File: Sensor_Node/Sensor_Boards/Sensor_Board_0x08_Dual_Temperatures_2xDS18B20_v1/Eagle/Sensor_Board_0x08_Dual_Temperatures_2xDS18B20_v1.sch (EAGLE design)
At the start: 16 parts, among them J2 1x3 RA Female .1", J3 1x3 RA Female .1", J4 ARDUINO_ISP, U2 ATMEGA328P_TQFP, Y1 8MHZ

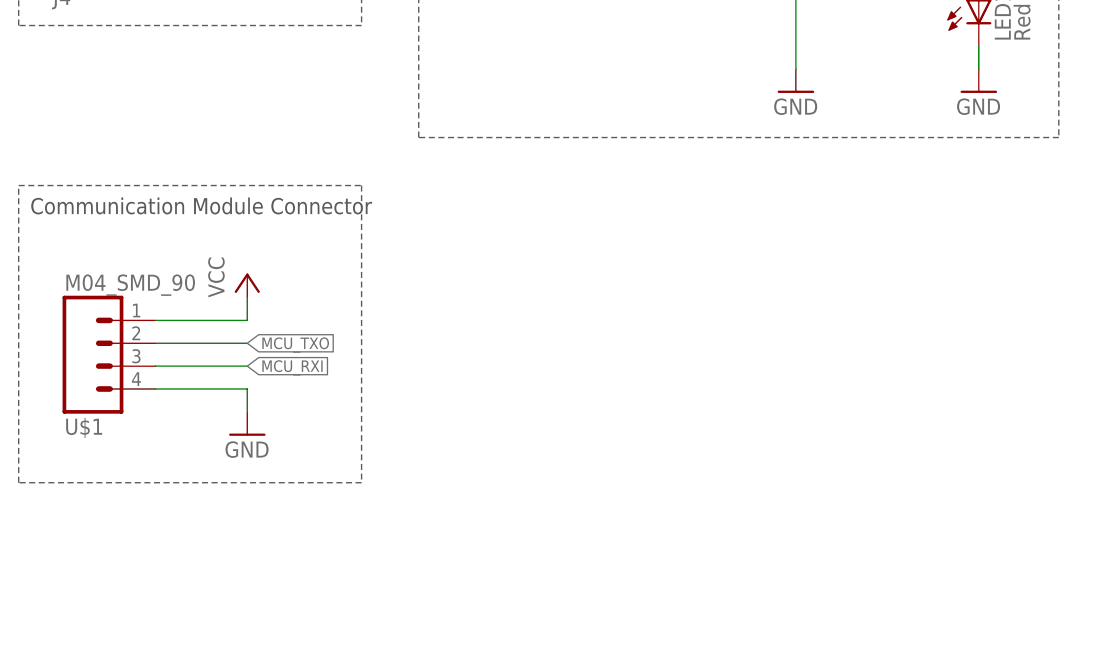
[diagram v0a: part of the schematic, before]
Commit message: Changes on SensModule 2xDS18B20
- added pogopin programming connector
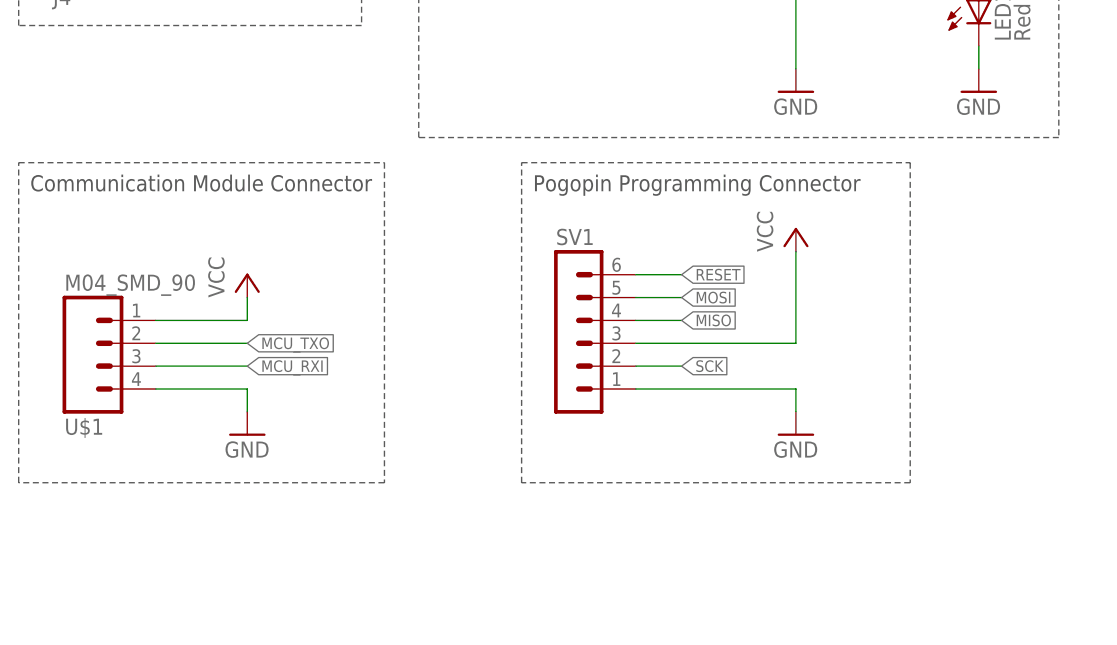
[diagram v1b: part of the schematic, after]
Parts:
- added SV1: (no value), con-lstb:MA06-1
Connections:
- net GND: now also SV1.1
- net MISO: now also SV1.4
- net MOSI: now also SV1.5
- net RESET: now also SV1.6
- net SCK: now also SV1.2
- net VCC: now also SV1.3
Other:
- note added: "Pogopin Programming Connector"
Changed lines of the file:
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@@
 <layers>
 <layer number="1" name="Top" color="4" fill="1" visible="no" active="no"/>
+<layer number="2" name="Route2" color="1" fill="3" visible="no" active="no"/>
+<layer number="3" name="Route3" color="4" fill="3" visible="no" active="no"/>
+<layer number="4" name="Route4" color="1" fill="4" visible="no" active="no"/>
+<layer number="5" name="Route5" color="4" fill="4" visible="no" active="no"/>
+<layer number="6" name="Route6" color="1" fill="8" visible="no" active="no"/>
+<layer number="7" name="Route7" color="4" fill="8" visible="no" active="no"/>
+<layer number="8" name="Route8" color="1" fill="2" visible="no" active="no"/>
+<layer number="9" name="Route9" color="4" fill="2" visible="no" active="no"/>
+<layer number="10" name="Route10" color="1" fill="7" visible="no" active="no"/>
+<layer number="11" name="Route11" color="4" fill="7" visible="no" active="no"/>
+<layer number="12" name="Route12" color="1" fill="5" visible="no" active="no"/>
+<layer number="13" name="Route13" color="4" fill="5" visible="no" active="no"/>
+<layer number="14" name="Route14" color="1" fill="6" visible="no" active="no"/>
+<layer number="15" name="Route15" color="4" fill="6" visible="no" active="no"/>
 <layer number="16" name="Bottom" color="1" fill="1" visible="no" active="no"/>
 <layer number="17" name="Pads" color="2" fill="1" visible="no" active="no"/>
@@
 <part name="U$16" library="myownthings" deviceset="N/C" device=""/>
 <part name="U$17" library="myownthings" deviceset="N/C" device=""/>
+<part name="SV1" library="con-lstb" deviceset="MA06-1" device=""/>
+<part name="P+8" library="supply1" deviceset="VCC" device=""/>
+<part name="GND3" library="SparkFun-Aesthetics" deviceset="GND" device=""/>
 </parts>
 <sheets>
@@
 <wire x1="125.73" y1="200.66" x2="7.62" y2="200.66" width="0.1524" layer="97" style="shortdash"/>
 <text x="8.89" y="197.485" size="1.778" layer="97">ATmega328</text>
-<wire x1="7.62" y1="30.226" x2="7.62" y2="63.246" width="0.1524" layer="97" style="shortdash"/>
-<wire x1="7.62" y1="63.246" x2="45.72" y2="63.246" width="0.1524" layer="97" style="shortdash"/>
-<wire x1="45.72" y1="63.246" x2="45.72" y2="30.226" width="0.1524" layer="97" style="shortdash"/>
-<wire x1="45.72" y1="30.226" x2="7.62" y2="30.226" width="0.1524" layer="97" style="shortdash"/>
-<text x="8.89" y="60.071" size="1.778" layer="97">Communication Module Connector</text>
+<wire x1="7.62" y1="30.226" x2="7.62" y2="65.786" width="0.1524" layer="97" style="shortdash"/>
+<wire x1="7.62" y1="65.786" x2="48.26" y2="65.786" width="0.1524" layer="97" style="shortdash"/>
+<wire x1="48.26" y1="65.786" x2="48.26" y2="30.226" width="0.1524" layer="97" style="shortdash"/>
+<wire x1="48.26" y1="30.226" x2="7.62" y2="30.226" width="0.1524" layer="97" style="shortdash"/>
+<text x="8.89" y="62.611" size="1.778" layer="97">Communication Module Connector</text>
 <wire x1="200.66" y1="152.4" x2="134.62" y2="152.4" width="0.1524" layer="97" style="shortdash"/>
 <wire x1="134.62" y1="88.9" x2="134.62" y2="152.4" width="0.1524" layer="97" style="shortdash"/>
@@
 <text x="224.505775" y="11.52471875" size="2.54" layer="94" font="vector">Sensor Board - 2xDS18B20</text>
 <text x="278.465165625" y="1.12011875" size="2.54" layer="94" font="vector">1.0</text>
+<wire x1="63.5" y1="30.226" x2="63.5" y2="65.786" width="0.1524" layer="97" style="shortdash"/>
+<wire x1="63.5" y1="65.786" x2="106.68" y2="65.786" width="0.1524" layer="97" style="shortdash"/>
+<wire x1="106.68" y1="65.786" x2="106.68" y2="30.226" width="0.1524" layer="97" style="shortdash"/>
+<wire x1="106.68" y1="30.226" x2="63.5" y2="30.226" width="0.1524" layer="97" style="shortdash"/>
+<text x="64.77" y="62.611" size="1.778" layer="97">Pogopin Programming Connector</text>
 </plain>
 <instances>
@@
 <instance part="U$16" gate="G$1" x="106.68" y="91.44"/>
 <instance part="U$17" gate="G$1" x="106.68" y="88.9"/>
+<instance part="SV1" gate="1" x="68.58" y="48.26"/>
+<instance part="P+8" gate="VCC" x="93.98" y="58.42"/>
+<instance part="GND3" gate="1" x="93.98" y="35.56"/>
 </instances>
 <busses>
@@
 <junction x="33.02" y="132.08"/>
 <junction x="33.02" y="129.54"/>
+</segment>
+<segment>
+<pinref part="SV1" gate="1" pin="1"/>
+<pinref part="GND3" gate="1" pin="GND"/>
+<wire x1="76.2" y1="40.64" x2="93.98" y2="40.64" width="0.1524" layer="91"/>
+<wire x1="93.98" y1="40.64" x2="93.98" y2="38.1" width="0.1524" layer="91"/>
 </segment>
 </net>
@@
 <wire x1="93.98" y1="93.98" x2="96.52" y2="93.98" width="0.1524" layer="91"/>
 </segment>
+<segment>
+<pinref part="P+8" gate="VCC" pin="VCC"/>
+<wire x1="93.98" y1="55.88" x2="93.98" y2="45.72" width="0.1524" layer="91"/>
+<pinref part="SV1" gate="1" pin="3"/>
+<wire x1="93.98" y1="45.72" x2="76.2" y2="45.72" width="0.1524" layer="91"/>
+</segment>
 </net>
 <net name="RESET" class="0">
@@
 <pinref part="J4" gate="G$1" pin="RST"/>
 </segment>
+<segment>
+<pinref part="SV1" gate="1" pin="6"/>
+<wire x1="76.2" y1="53.34" x2="81.28" y2="53.34" width="0.1524" layer="91"/>
+<label x="81.28" y="53.34" size="1.27" layer="95" xref="yes"/>
+</segment>
 </net>
 <net name="SCK" class="0">
@@
 <pinref part="U2" gate="U$1" pin="PB5(SCK)"/>
 </segment>
+<segment>
+<pinref part="SV1" gate="1" pin="2"/>
+<wire x1="76.2" y1="43.18" x2="81.28" y2="43.18" width="0.1524" layer="91"/>
+<label x="81.28" y="43.18" size="1.27" layer="95" xref="yes"/>
+</segment>
 </net>
 <net name="MISO" class="0">
@@
 <pinref part="U2" gate="U$1" pin="PB4(MISO)"/>
 </segment>
+<segment>
+<pinref part="SV1" gate="1" pin="4"/>
+<wire x1="76.2" y1="48.26" x2="81.28" y2="48.26" width="0.1524" layer="91"/>
+<label x="81.28" y="48.26" size="1.27" layer="95" xref="yes"/>
+</segment>
 </net>
 <net name="MOSI" class="0">
@@
 <pinref part="U2" gate="U$1" pin="PB3(MOSI/OC2)"/>
 </segment>
+<segment>
+<pinref part="SV1" gate="1" pin="5"/>
+<wire x1="76.2" y1="50.8" x2="81.28" y2="50.8" width="0.1524" layer="91"/>
+<label x="81.28" y="50.8" size="1.27" layer="95" xref="yes"/>
+</segment>
 </net>

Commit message: Changes on all boards
- added capacitor on reset-path
- changed order of pogopin programmer pins

Pulse-Board:
- Deleted input-jumper. Currently one interrupt-pin missing, so print is
not yet routed.
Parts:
- added C1: 100n, eagle-ltspice:C
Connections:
- new net N$4: C1.2, R5.1, S1.RIGHT, U2.PC6(/RESET)
- net MISO: now also SV1.6; no longer SV1.4
- net MOSI: now also SV1.2; no longer SV1.5
- net RESET: now also C1.1, SV1.4; no longer R5.1, S1.RIGHT, SV1.6, U2.PC6(/RESET)
- net SCK: now also SV1.5; no longer SV1.2
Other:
- moved on the sheet: C10, C9, R5, S1, U2, Y1

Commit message: Updated schematic description
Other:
- note added: "Sensor Board - 2xDS18B20 (0x08)"
- note removed: "Sensor Board - 2xDS18B20"
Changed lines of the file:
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@@
 <wire x1="200.66" y1="88.9" x2="134.62" y2="88.9" width="0.1524" layer="97" style="shortdash"/>
 <text x="137.16" y="147.32" size="1.778" layer="97">DS18B20</text>
-<text x="224.505775" y="11.52471875" size="2.54" layer="94" font="vector">Sensor Board - 2xDS18B20</text>
+<text x="224.505775" y="11.52471875" size="2.54" layer="94" font="vector">Sensor Board - 2xDS18B20 (0x08)</text>
 <text x="278.465165625" y="1.12011875" size="2.54" layer="94" font="vector">1.0</text>
 <wire x1="63.5" y1="30.226" x2="63.5" y2="65.786" width="0.1524" layer="97" style="shortdash"/>

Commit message: Finished some boards.
- Minor changes on all boards except
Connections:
- new net FTDI_RXI: SV1.4, U2.PD0(RXD)
- new net FTDI_TXO: SV1.5, U2.PD1(TXD)
- net GND: now also SV1.2
- net MCU_RXI: now also U2.PD7(AIN1); no longer U2.PD0(RXD)
- net MCU_TXO: now also U2.PD6(AIN0); no longer U2.PD1(TXD)
- net MISO: no longer SV1.6
- net MOSI: no longer SV1.2
- net RESET: now also SV1.6; no longer SV1.4
- net SCK: no longer SV1.5
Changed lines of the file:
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@@
 <setting verticaltext="up"/>
 </settings>
-<grid distance="0.1" unitdist="inch" unit="inch" style="lines" multiple="1" display="no" altdistance="0.01" altunitdist="inch" altunit="inch"/>
+<grid distance="0.05" unitdist="inch" unit="inch" style="lines" multiple="1" display="yes" altdistance="0.01" altunitdist="inch" altunit="inch"/>
 <layers>
 <layer number="1" name="Top" color="4" fill="1" visible="no" active="no"/>
@@
 <part name="U$8" library="myownthings" deviceset="N/C" device=""/>
 <part name="U$9" library="myownthings" deviceset="N/C" device=""/>
-<part name="U$10" library="myownthings" deviceset="N/C" device=""/>
-<part name="U$11" library="myownthings" deviceset="N/C" device=""/>
 <part name="U$12" library="myownthings" deviceset="N/C" device=""/>
 <part name="U$13" library="myownthings" deviceset="N/C" device=""/>
@@
 <wire x1="45.72" y1="81.026" x2="7.62" y2="81.026" width="0.1524" layer="97" style="shortdash"/>
 <text x="8.89" y="110.871" size="1.778" layer="97">Programming Connector</text>
-<wire x1="6.35" y1="204.47" x2="7.62" y2="118.11" width="0.1524" layer="97" style="shortdash"/>
-<wire x1="7.62" y1="118.11" x2="125.73" y2="118.11" width="0.1524" layer="97" style="shortdash"/>
-<wire x1="125.73" y1="118.11" x2="124.46" y2="204.47" width="0.1524" layer="97" style="shortdash"/>
-<wire x1="124.46" y1="204.47" x2="6.35" y2="204.47" width="0.1524" layer="97" style="shortdash"/>
+<wire x1="7.62" y1="204.47" x2="7.62" y2="118.11" width="0.1524" layer="97" style="shortdash"/>
+<wire x1="7.62" y1="118.11" x2="124.46" y2="118.11" width="0.1524" layer="97" style="shortdash"/>
+<wire x1="124.46" y1="118.11" x2="124.46" y2="204.47" width="0.1524" layer="97" style="shortdash"/>
+<wire x1="124.46" y1="204.47" x2="7.62" y2="204.47" width="0.1524" layer="97" style="shortdash"/>
 <text x="8.89" y="201.295" size="1.778" layer="97">ATmega328</text>
 <wire x1="7.62" y1="30.226" x2="7.62" y2="65.786" width="0.1524" layer="97" style="shortdash"/>
@@
 <instance part="U$8" gate="G$1" x="102.87" y="156.21"/>
 <instance part="U$9" gate="G$1" x="102.87" y="153.67"/>
-<instance part="U$10" gate="G$1" x="102.87" y="151.13"/>
-<instance part="U$11" gate="G$1" x="102.87" y="148.59"/>
 <instance part="U$12" gate="G$1" x="102.87" y="146.05"/>
 <instance part="U$13" gate="G$1" x="102.87" y="143.51"/>
@@
 <wire x1="76.2" y1="40.64" x2="93.98" y2="40.64" width="0.1524" layer="91"/>
 <wire x1="93.98" y1="40.64" x2="93.98" y2="38.1" width="0.1524" layer="91"/>
+<pinref part="SV1" gate="1" pin="2"/>
+<wire x1="76.2" y1="43.18" x2="93.98" y2="43.18" width="0.1524" layer="91"/>
+<wire x1="93.98" y1="43.18" x2="93.98" y2="40.64" width="0.1524" layer="91"/>
+<junction x="93.98" y="40.64"/>
 </segment>
 </net>
@@
 </segment>
 <segment>
-<pinref part="SV1" gate="1" pin="4"/>
-<wire x1="76.2" y1="48.26" x2="81.28" y2="48.26" width="0.1524" layer="91"/>
-<label x="81.28" y="48.26" size="1.27" layer="95" xref="yes"/>
+<pinref part="SV1" gate="1" pin="6"/>
+<wire x1="76.2" y1="53.34" x2="81.28" y2="53.34" width="0.1524" layer="91"/>
+<label x="81.28" y="53.34" size="1.27" layer="95" xref="yes"/>
 </segment>
 </net>
@@
 <pinref part="U2" gate="U$1" pin="PB5(SCK)"/>
 </segment>
-<segment>
-<pinref part="SV1" gate="1" pin="5"/>
-<wire x1="76.2" y1="50.8" x2="81.28" y2="50.8" width="0.1524" layer="91"/>
-<label x="81.28" y="50.8" size="1.27" layer="95" xref="yes"/>
-</segment>
 </net>
 <net name="MISO" class="0">
@@
 <pinref part="U2" gate="U$1" pin="PB4(MISO)"/>
 </segment>
-<segment>
-<pinref part="SV1" gate="1" pin="6"/>
-<wire x1="76.2" y1="53.34" x2="81.28" y2="53.34" width="0.1524" layer="91"/>
-<label x="81.28" y="53.34" size="1.27" layer="95" xref="yes"/>
-</segment>
 </net>
 <net name="MOSI" class="0">
@@
 <pinref part="U2" gate="U$1" pin="PB3(MOSI/OC2)"/>
 </segment>
-<segment>
-<pinref part="SV1" gate="1" pin="2"/>
-<wire x1="76.2" y1="43.18" x2="81.28" y2="43.18" width="0.1524" layer="91"/>
-<label x="81.28" y="43.18" size="1.27" layer="95" xref="yes"/>
-</segment>
 </net>
 <net name="MCU_TXO" class="0">
-<segment>
-<wire x1="102.87" y1="163.83" x2="105.41" y2="163.83" width="0.1524" layer="91"/>
-<label x="105.41" y="163.83" size="1.27" layer="95" xref="yes"/>
-<pinref part="U2" gate="U$1" pin="PD1(TXD)"/>
-</segment>
 <segment>
 <label x="33.02" y="45.72" size="1.27" layer="95" xref="yes"/>
@@
 <wire x1="33.02" y1="45.72" x2="22.86" y2="45.72" width="0.1524" layer="91"/>
 </segment>
+<segment>
+<pinref part="U2" gate="U$1" pin="PD6(AIN0)"/>
+<wire x1="102.87" y1="151.13" x2="105.41" y2="151.13" width="0.1524" layer="91"/>
+<label x="105.41" y="151.13" size="1.27" layer="95" xref="yes"/>
+</segment>
 </net>
 <net name="L1" class="0">
@@
 <net name="MCU_RXI" class="0">
 <segment>
-<wire x1="102.87" y1="166.37" x2="105.41" y2="166.37" width="0.1524" layer="91"/>
-<label x="105.41" y="166.37" size="1.27" layer="95" xref="yes"/>
-<pinref part="U2" gate="U$1" pin="PD0(RXD)"/>
-</segment>
-<segment>
 <label x="33.02" y="43.18" size="1.27" layer="95" xref="yes"/>
 <pinref part="U$1" gate="G$1" pin="3"/>
 <wire x1="33.02" y1="43.18" x2="22.86" y2="43.18" width="0.1524" layer="91"/>
+</segment>
+<segment>
+<pinref part="U2" gate="U$1" pin="PD7(AIN1)"/>
+<wire x1="102.87" y1="148.59" x2="105.41" y2="148.59" width="0.1524" layer="91"/>
+<label x="105.41" y="148.59" size="1.27" layer="95" xref="yes"/>
 </segment>
 </net>
@@
 </segment>
 </net>
+<net name="FTDI_TXO" class="0">
+<segment>
+<pinref part="SV1" gate="1" pin="5"/>
+<wire x1="76.2" y1="50.8" x2="81.28" y2="50.8" width="0.1524" layer="91"/>
+<label x="81.28" y="50.8" size="1.27" layer="95" xref="yes"/>
+</segment>
+<segment>
+<wire x1="102.87" y1="163.83" x2="105.41" y2="163.83" width="0.1524" layer="91"/>
+<label x="105.41" y="163.83" size="1.27" layer="95" xref="yes"/>
+<pinref part="U2" gate="U$1" pin="PD1(TXD)"/>
+</segment>
+</net>
+<net name="FTDI_RXI" class="0">
+<segment>
+<pinref part="SV1" gate="1" pin="4"/>
+<wire x1="76.2" y1="48.26" x2="81.28" y2="48.26" width="0.1524" layer="91"/>
+<label x="81.28" y="48.26" size="1.27" layer="95" xref="yes"/>
+</segment>
+<segment>
+<wire x1="102.87" y1="166.37" x2="105.41" y2="166.37" width="0.1524" layer="91"/>
+<label x="105.41" y="166.37" size="1.27" layer="95" xref="yes"/>
+<pinref part="U2" gate="U$1" pin="PD0(RXD)"/>
+</segment>
+</net>

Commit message: DS18B20 - Board
- adjusted reset path
- minor changes in layout
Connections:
- removed net N$4: C1.2, R5.1, S1.RIGHT, U2.PC6(/RESET)
- new net FTDI_RESET: C1.1, SV1.6
- net RESET: now also C1.2, R5.1, S1.RIGHT, U2.PC6(/RESET); no longer C1.1, SV1.6
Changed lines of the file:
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@@
 <?xml version="1.0" encoding="utf-8"?>
 <!DOCTYPE eagle SYSTEM "eagle.dtd">
-<eagle version="8.1.1">
+<eagle version="8.2.2">
 <drawing>
 <settings>
@@
 <setting verticaltext="up"/>
 </settings>
-<grid distance="0.05" unitdist="inch" unit="inch" style="lines" multiple="1" display="yes" altdistance="0.01" altunitdist="inch" altunit="inch"/>
+<grid distance="0.1" unitdist="inch" unit="inch" style="lines" multiple="1" display="no" altdistance="0.01" altunitdist="inch" altunit="inch"/>
 <layers>
 <layer number="1" name="Top" color="4" fill="1" visible="no" active="no"/>
@@
 </segment>
 <segment>
-<pinref part="C1" gate="G$1" pin="1"/>
-<wire x1="27.94" y1="186.69" x2="22.86" y2="186.69" width="0.1524" layer="91"/>
-<label x="22.86" y="186.69" size="1.778" layer="95" rot="R180" xref="yes"/>
-</segment>
-<segment>
-<pinref part="SV1" gate="1" pin="6"/>
-<wire x1="76.2" y1="53.34" x2="81.28" y2="53.34" width="0.1524" layer="91"/>
-<label x="81.28" y="53.34" size="1.27" layer="95" xref="yes"/>
+<pinref part="R5" gate="G$1" pin="1"/>
+<pinref part="S1" gate="G$1" pin="RIGHT"/>
+<wire x1="41.91" y1="189.23" x2="41.91" y2="186.69" width="0.1524" layer="91"/>
+<pinref part="U2" gate="U$1" pin="PC6(/RESET)"/>
+<wire x1="41.91" y1="186.69" x2="41.91" y2="184.15" width="0.1524" layer="91"/>
+<wire x1="54.61" y1="186.69" x2="48.895" y2="186.69" width="0.1524" layer="91"/>
+<junction x="41.91" y="186.69"/>
+<pinref part="C1" gate="G$1" pin="2"/>
+<wire x1="48.895" y1="186.69" x2="41.91" y2="186.69" width="0.1524" layer="91"/>
+<wire x1="41.91" y1="186.69" x2="35.56" y2="186.69" width="0.1524" layer="91"/>
+<wire x1="48.895" y1="186.69" x2="48.895" y2="194.691" width="0.1524" layer="91"/>
+<junction x="48.895" y="186.69"/>
+<wire x1="48.895" y1="194.691" x2="57.658" y2="194.691" width="0.1524" layer="91"/>
+<wire x1="57.658" y1="194.691" x2="57.658" y2="194.564" width="0.1524" layer="91"/>
+<label x="57.658" y="194.564" size="1.27" layer="95" xref="yes"/>
 </segment>
 </net>
@@
 </segment>
 </net>
-<net name="N$4" class="0">
-<segment>
-<pinref part="R5" gate="G$1" pin="1"/>
-<pinref part="S1" gate="G$1" pin="RIGHT"/>
-<wire x1="41.91" y1="189.23" x2="41.91" y2="186.69" width="0.1524" layer="91"/>
-<pinref part="U2" gate="U$1" pin="PC6(/RESET)"/>
-<wire x1="41.91" y1="186.69" x2="41.91" y2="184.15" width="0.1524" layer="91"/>
-<wire x1="54.61" y1="186.69" x2="41.91" y2="186.69" width="0.1524" layer="91"/>
-<junction x="41.91" y="186.69"/>
-<pinref part="C1" gate="G$1" pin="2"/>
-<wire x1="41.91" y1="186.69" x2="35.56" y2="186.69" width="0.1524" layer="91"/>
-</segment>
-</net>
 <net name="FTDI_TXO" class="0">
 <segment>
@@
 </segment>
 </net>
+<net name="FTDI_RESET" class="0">
+<segment>
+<pinref part="SV1" gate="1" pin="6"/>
+<wire x1="76.2" y1="53.34" x2="81.28" y2="53.34" width="0.1524" layer="91"/>
+<label x="81.28" y="53.34" size="1.27" layer="95" xref="yes"/>
+</segment>
+<segment>
+<pinref part="C1" gate="G$1" pin="1"/>
+<wire x1="27.94" y1="186.69" x2="22.86" y2="186.69" width="0.1524" layer="91"/>
+<label x="22.86" y="186.69" size="1.27" layer="95" rot="R180" xref="yes"/>
+</segment>
+</net>

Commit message: Updated Prototyping Board & DS18B20 Board
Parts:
- removed R8: 330, SparkFun-Passives:RESISTOR0805-RES
- added R4: 4.7k, SparkFun-Passives:RESISTOR0805-RES
- R2: value 4.7k -> 10k
- R3: value 4.7k -> 330
- R5: value 10k -> 4.7k
- renumbered C10 to C3, C9 to C2, R6 to R1
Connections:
- net DS18B20_DATA_1: now also R4.1; no longer R2.1
- net DS18B20_DATA_2: now also R5.1; no longer R3.1
- net L1: now also R3.2, U2.PB2(SS/OC1B); no longer R8.2, U2.PC0(ADC0)
- net N$30: now also R3.1; no longer R8.1
- net RESET: now also R2.1; no longer R5.1
- net VCC: now also R4.2; no longer R3.2
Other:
- moved on the sheet: R2, R3, R5
